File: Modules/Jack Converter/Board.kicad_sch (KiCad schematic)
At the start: 38 parts, among them J1 TS_Jack_3.5mm, J10 TS_Jack_6.35mm, J100 IDC_02x08, J11 TS_Jack_3.5mm, J12 TS_Jack_6.35mm, J13 TS_Jack_3.5mm, J14 TS_Jack_6.35mm, J15 TS_Jack_3.5mm, J16 TS_Jack_6.35mm, J17 TS_Jack_3.5mm, J18 TS_Jack_6.35mm, J19 TS_Jack_3.5mm, J2 TS_Jack_6.35mm, J20 TS_Jack_6.35mm, J21 TS_Jack_3.5mm, J22 TS_Jack_6.35mm, J3 TS_Jack_3.5mm, J4 TS_Jack_6.35mm, J5 TS_Jack_3.5mm, J6 TS_Jack_6.35mm, J7 TS_Jack_3.5mm, J8 TS_Jack_6.35mm, J9 TS_Jack_3.5mm, SW1 SW_DPDT, SW2 SW_DPDT, SW3 SW_DPDT, SW4 SW_DPDT

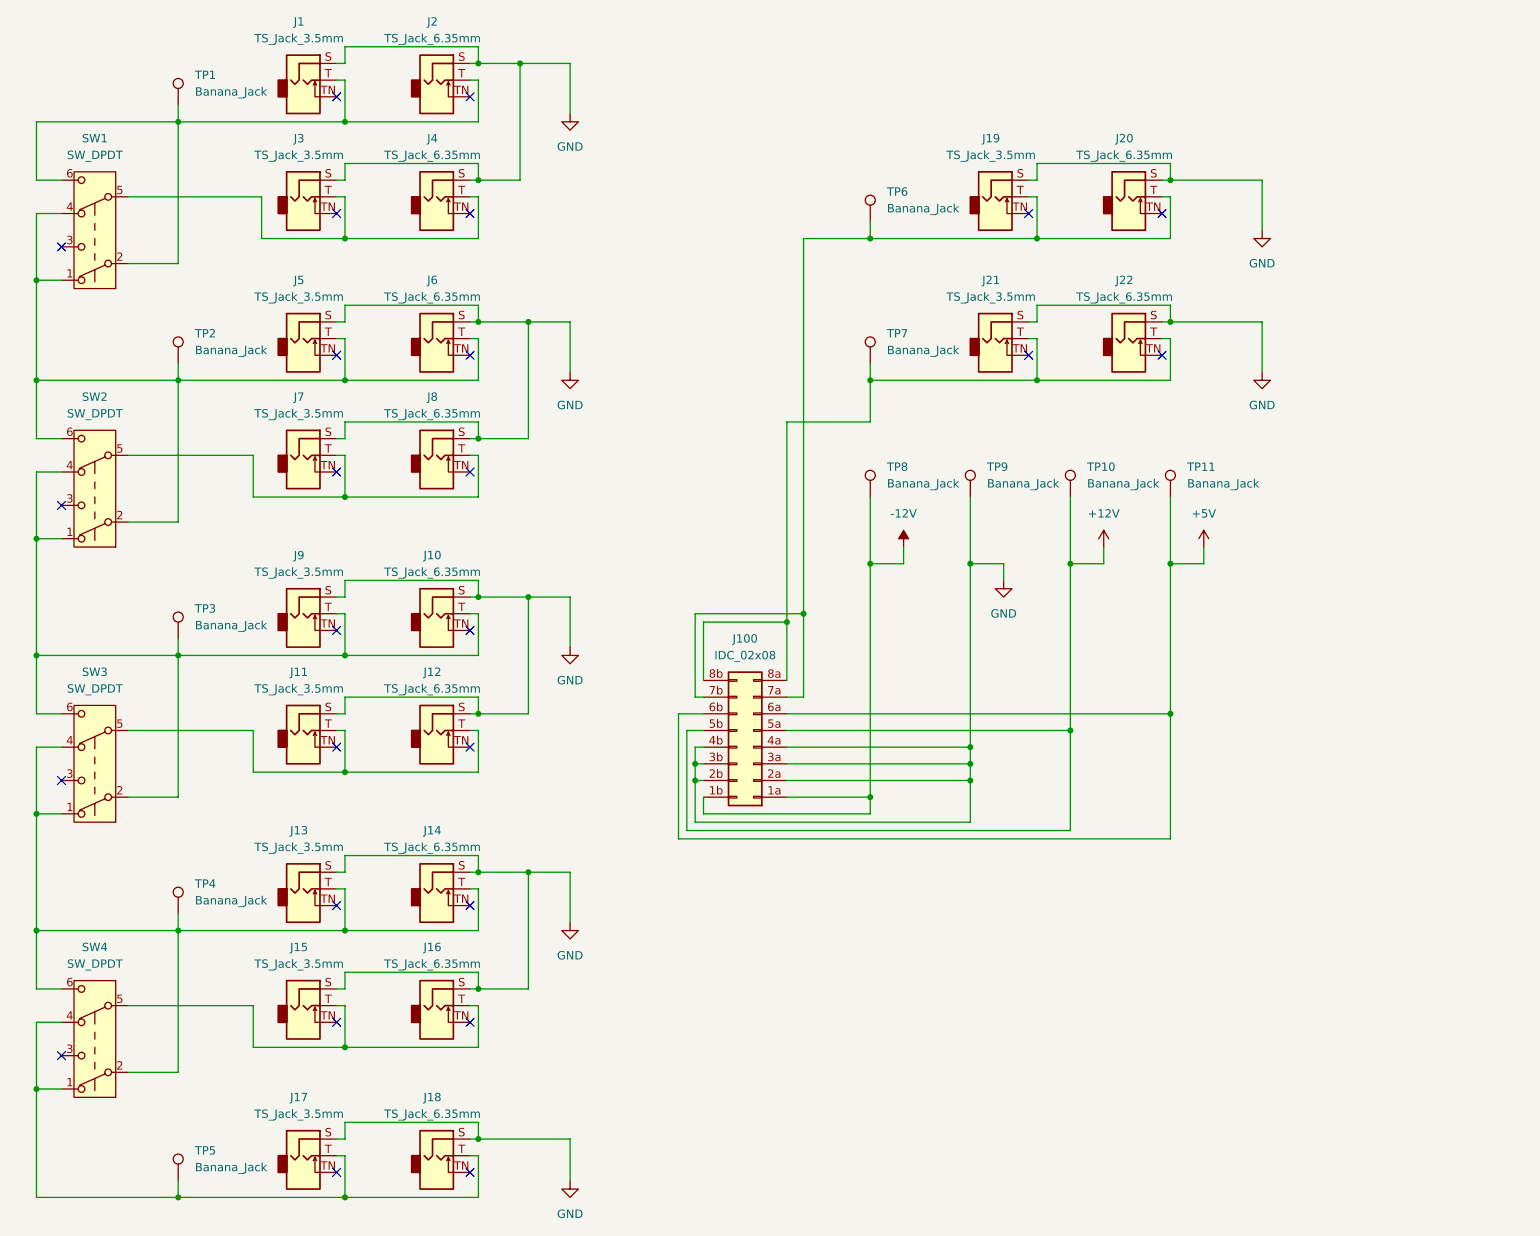
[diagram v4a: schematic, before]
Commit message: Updated symbols to use Synth_Stuff library
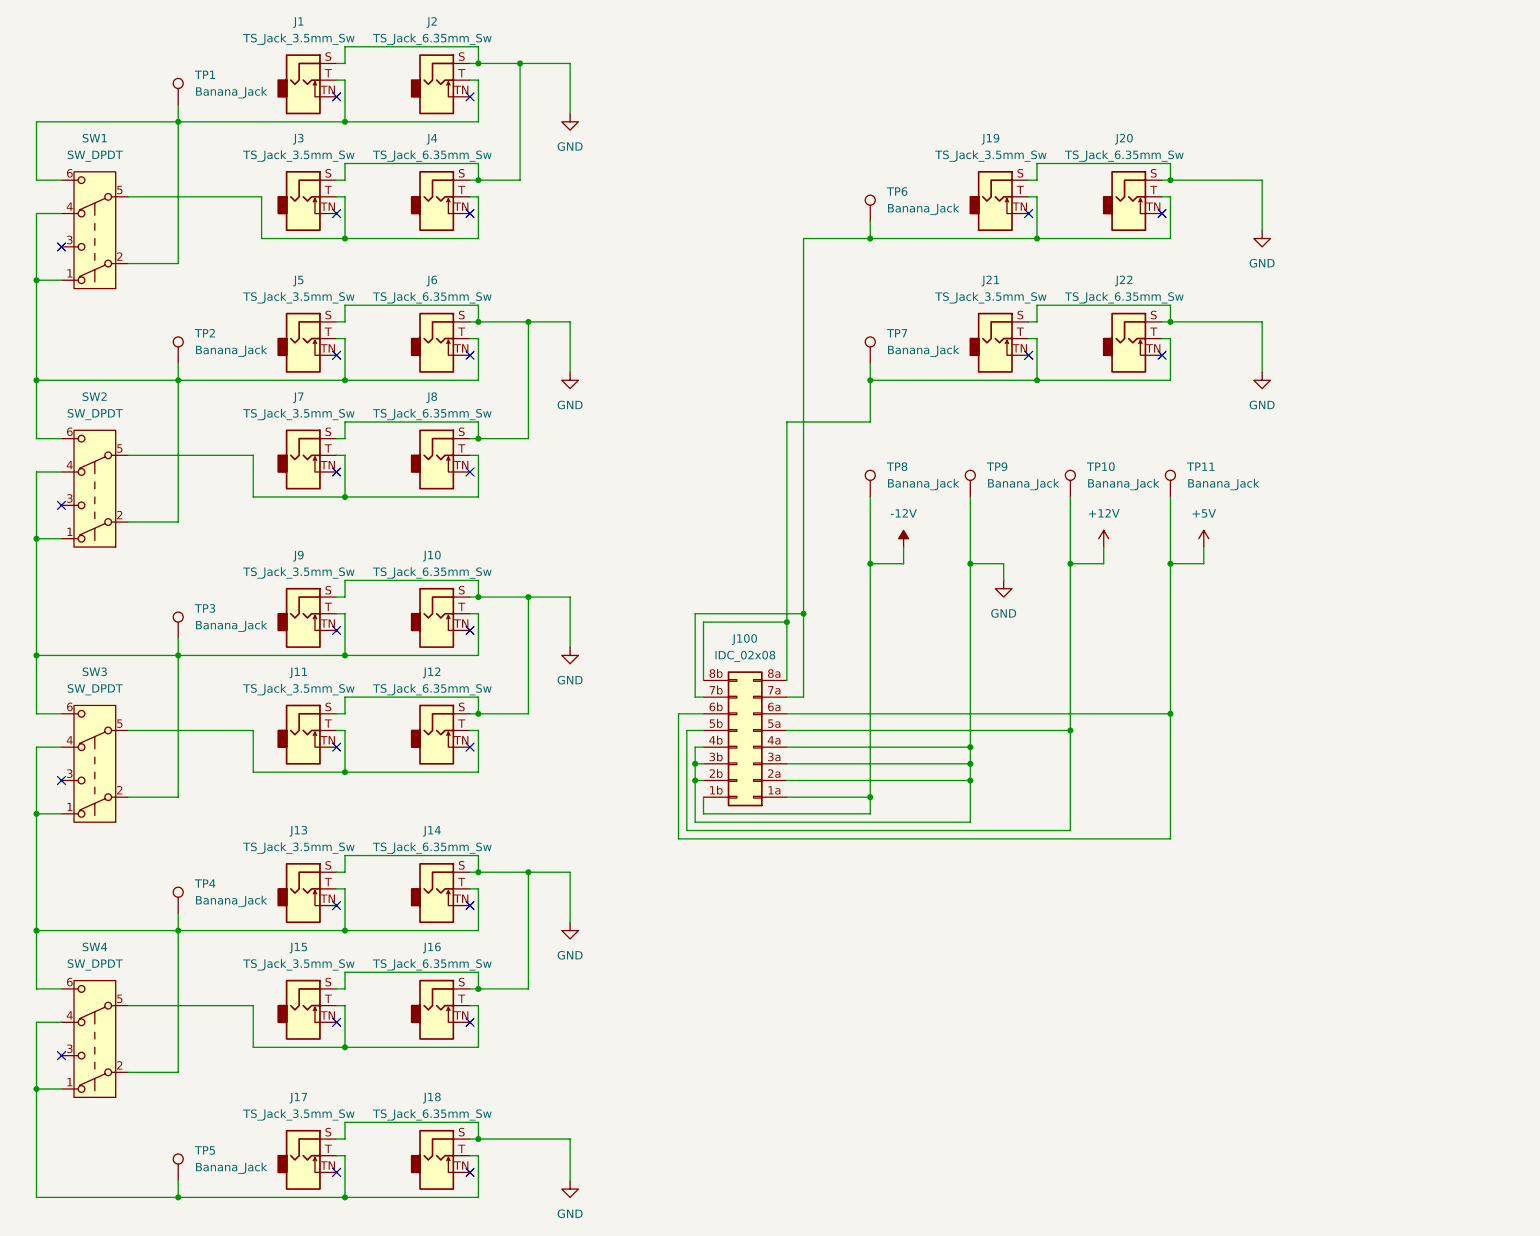
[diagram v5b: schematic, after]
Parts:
- J1, J11, J13, J15, J17, J19, J21, J3, J5, J7, J9: value TS_Jack_3.5mm -> TS_Jack_3.5mm_Sw; symbol Connector_Audio:AudioJack2_SwitchT -> Synth_Stuff:TS_Jack_3.5mm_Sw
- J10, J12, J14, J16, J18, J2, J20, J22, J4, J6, J8: value TS_Jack_6.35mm -> TS_Jack_6.35mm_Sw; symbol Connector_Audio:AudioJack2_SwitchT -> Synth_Stuff:TS_Jack_6.35mm_Sw
- J100: footprint (none) -> Connector_IDC:IDC-Header_2x08_P2.54mm_Vertical; symbol Connector_Generic:Conn_02x08_Row_Letter_Last -> Synth_Stuff:Eurorack_Power_Connector_16Pin
- SW1, SW2, SW3, SW4: symbol Switch:SW_Push_DPDT -> Synth_Stuff:Switch_DPDT
- TP1, TP10, TP11, TP2, TP3, TP4, TP5, TP6, TP7, TP8, TP9: symbol Connector:TestPoint -> Synth_Stuff:Banana_Jack

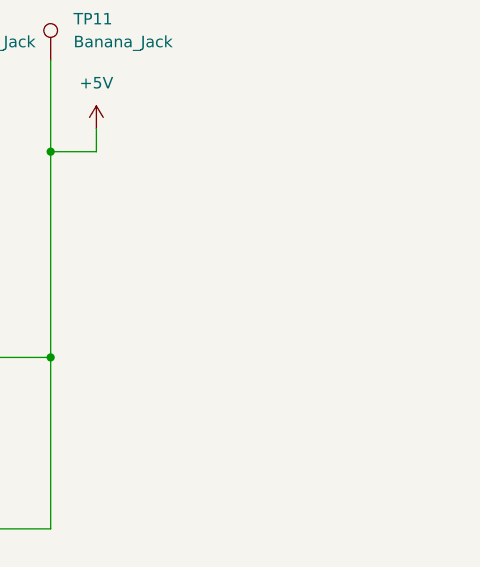
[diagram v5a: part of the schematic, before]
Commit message: Added SynthStuff library to Jack Converter project
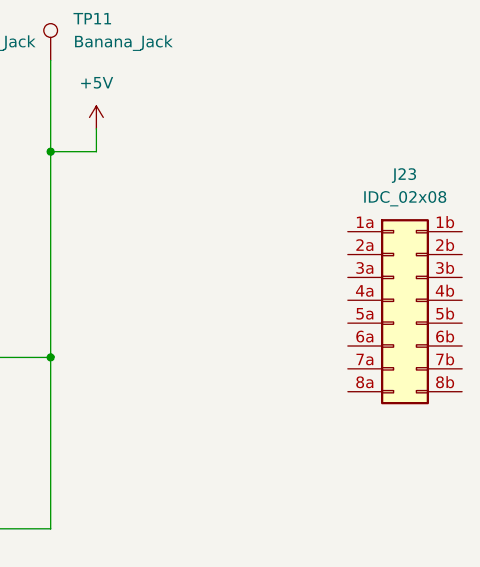
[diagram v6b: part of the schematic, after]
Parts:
- added J23: IDC_02x08, Connector_IDC:IDC-Header_2x08_P2.54mm_Vertical, symbol Synth_Stuff:Eurorack_Power_Connector_16Pin
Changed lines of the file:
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@@
+	)
+	(symbol
+		(lib_id "Synth_Stuff:Eurorack_Power_Connector_16Pin")
+		(at 243.84 114.3 0)
+		(unit 1)
+		(exclude_from_sim no)
+		(in_bom yes)
+		(on_board yes)
+		(dnp no)
+		(fields_autoplaced yes)
+		(property "Reference" "J23"
+			(at 245.11 100.33 0)
+			(effects
+				(font
+					(size 1.27 1.27)
+				)
+			)
+		)
+		(property "Value" "IDC_02x08"
+			(at 245.11 102.87 0)
+			(effects
+				(font
+					(size 1.27 1.27)
+				)
+			)
+		)
+		(property "Footprint" "Connector_IDC:IDC-Header_2x08_P2.54mm_Vertical"
+			(at 243.84 114.3 0)
+			(effects
+				(font
+					(size 1.27 1.27)
+				)
+				(hide yes)
+			)
+		)
+		(property "Datasheet" "~"
+			(at 243.84 114.3 0)
+			(effects
+				(font
+					(size 1.27 1.27)
+				)
+				(hide yes)
+			)
+		)
+		(property "Description" "IDC jack, 2x8 pins, row a carries same signals as row b."
+			(at 243.84 114.3 0)
+			(effects
+				(font
+					(size 1.27 1.27)
+				)
+				(hide yes)
+			)
+		)
+		(pin "6b"
+		)
+		(pin "1b"
+		)
+		(pin "4b"
+		)
+		(pin "7b"
+		)
+		(pin "3a"
+		)
+		(pin "5b"
+		)
+		(pin "2a"
+		)
+		(pin "5a"
+		)
+		(pin "8a"
+		)
+		(pin "6a"
+		)
+		(pin "1a"
+		)
+		(pin "4a"
+		)
+		(pin "2b"
+		)
+		(pin "3b"
+		)
+		(pin "8b"
+		)
+		(pin "7a"
+		)
+		(instances
+			(project "Jack Converter"
+				(path "/b497d75e-0918-4e9c-ae43-36360bc031dc/01b3bf80-fded-40b5-ad81-2678b7ef607a"
+					(reference "J23")
+					(unit 1)
+				)
+			)
+		)
 	)
 	(symbol

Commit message: Testing change to submodule
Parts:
- removed J23: IDC_02x08, Connector_IDC:IDC-Header_2x08_P2.54mm_Vertical, symbol Synth_Stuff:Eurorack_Power_Connector_16Pin
- added J23: TS_Jack_6.35mm, symbol Synth_Stuff:TS_Jack_6.35mm
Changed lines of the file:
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@@
+	)
+	(symbol
+		(lib_id "Synth_Stuff:TS_Jack_6.35mm")
+		(at 251.46 62.23 0)
+		(unit 1)
+		(exclude_from_sim no)
+		(in_bom yes)
+		(on_board yes)
+		(dnp no)
+		(fields_autoplaced yes)
+		(property "Reference" "J23"
+			(at 250.825 53.34 0)
+			(effects
+				(font
+					(size 1.27 1.27)
+				)
+			)
+		)
+		(property "Value" "TS_Jack_6.35mm"
+			(at 250.825 55.88 0)
+			(effects
+				(font
+					(size 1.27 1.27)
+				)
+			)
+		)
+		(property "Footprint" ""
+			(at 251.46 62.23 0)
+			(effects
+				(font
+					(size 1.27 1.27)
+				)
+				(hide yes)
+			)
+		)
+		(property "Datasheet" "~"
+			(at 251.46 62.23 0)
+			(effects
+				(font
+					(size 1.27 1.27)
+				)
+				(hide yes)
+			)
+		)
+		(property "Description" "Audio Jack, 2 Poles (Mono / TS)"
+			(at 251.46 62.23 0)
+			(effects
+				(font
+					(size 1.27 1.27)
+				)
+				(hide yes)
+			)
+		)
+		(pin "T"
+		)
+		(pin "S"
+		)
+		(instances
+			(project "Jack Converter"
+				(path "/b497d75e-0918-4e9c-ae43-36360bc031dc/01b3bf80-fded-40b5-ad81-2678b7ef607a"
+					(reference "J23")
+					(unit 1)
+				)
+			)
+		)
 	)
 	(symbol
@@
 					(unit 1)
 				)
-			)
-		)
-	)
-	(symbol
-		(lib_id "Synth_Stuff:Eurorack_Power_Connector_16Pin")
-		(at 243.84 114.3 0)
-		(unit 1)
-		(exclude_from_sim no)
-		(in_bom yes)
-		(on_board yes)
-		(dnp no)
-		(fields_autoplaced yes)
-		(property "Reference" "J23"
-			(at 245.11 100.33 0)
-			(effects
-				(font
-					(size 1.27 1.27)
-				)
-			)
-		)
-		(property "Value" "IDC_02x08"
-			(at 245.11 102.87 0)
-			(effects
-				(font
-					(size 1.27 1.27)
-				)
-			)
-		)
-		(property "Footprint" "Connector_IDC:IDC-Header_2x08_P2.54mm_Vertical"
-			(at 243.84 114.3 0)
-			(effects
-				(font
-					(size 1.27 1.27)
-				)
-				(hide yes)
-			)
-		)
-		(property "Datasheet" "~"
-			(at 243.84 114.3 0)
-			(effects
-				(font
-					(size 1.27 1.27)
-				)
-				(hide yes)
-			)
-		)
-		(property "Description" "IDC jack, 2x8 pins, row a carries same signals as row b."
-			(at 243.84 114.3 0)
-			(effects
-				(font
-					(size 1.27 1.27)
-				)
-				(hide yes)
-			)
-		)
-		(pin "6b"
-		)
-		(pin "1b"
-		)
-		(pin "4b"
-		)
-		(pin "7b"
-		)
-		(pin "3a"
-		)
-		(pin "5b"
-		)
-		(pin "2a"
-		)
-		(pin "5a"
-		)
-		(pin "8a"
-		)
-		(pin "6a"
-		)
-		(pin "1a"
-		)
-		(pin "4a"
-		)
-		(pin "2b"
-		)
-		(pin "3b"
-		)
-		(pin "8b"
-		)
-		(pin "7a"
-		)
-		(instances
-			(project "Jack Converter"
-				(path "/b497d75e-0918-4e9c-ae43-36360bc031dc/01b3bf80-fded-40b5-ad81-2678b7ef607a"
-					(reference "J23")
-					(unit 1)
-				)
